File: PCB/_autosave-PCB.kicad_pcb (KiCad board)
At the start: 2 copper layers, 100 x 120 mm, 17 parts, among them SW1 SW_Push, SW2 SW_Push, SW3 SW_Push, SW4 SW_Push, SW5 SW_Push, SW6 SW_Push, U1 NodeMCU_1.0_(ESP-12E)

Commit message: Updated schematic after CMZ feedback
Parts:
- added H1: MountingHole_Pad, MountingHole:MountingHole_3.2mm_M3, F.Cu at (183.5, 30.1)
- added H2: MountingHole_Pad, MountingHole:MountingHole_3.2mm_M3, F.Cu at (91.5, 30.1)
- added H3: MountingHole_Pad, MountingHole:MountingHole_3.2mm_M3, F.Cu at (183.6, 142.1)
- added H4: MountingHole_Pad, MountingHole:MountingHole_3.2mm_M3, F.Cu at (91.5, 142.1)
- renumbered NHD to NHD-C12864A1Z-FSW-FBW-HTT1
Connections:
- net /Analog buttons renamed BUTTONS
- net Net-(BZ1-+) renamed BUZZER
- net Net-(NHD-C12864A1Z-FSW-FBW-HTT1-A0) renamed A0
- net Net-(NHD-C12864A1Z-FSW-FBW-HTT1-LED+) renamed 3.3 (16)
- net Net-(NHD-C12864A1Z-FSW-FBW-HTT1-SCL) renamed SCL
- net Net-(NHD-C12864A1Z-FSW-FBW-HTT1-SI) renamed SI
- net Net-(NHD-C12864A1Z-FSW-FBW-HTT1-VDD) renamed 3.3 (25)
- net Net-(NHD-C12864A1Z-FSW-FBW-HTT1-~{CS}) renamed ~{CS}
- net Net-(U1-RX(DPIO3)) renamed SW1
- net Net-(U1-TX(GPIO1)) renamed SW2
- net VCC renamed +5V
- D1 pad 2: Net-(D1-A) -> RED
- D2 pad 2: Net-(D2-A) -> GREEN
- EM4100 pad 1: Net-(EM4100-TX) -> HV2
- EM4100 pad 2: Net-(EM4100-RX) -> HV1
- NHD-C12864A1Z-FSW-FBW-HTT1 pad 5: Net-(NHD-C12864A1Z-FSW-FBW-HTT1-~{RESET}) -> ~{RESET}
- U1 pad 26: Net-(D2-A) -> ~{RESET}
- U1 pad 27: Net-(D1-A) -> LV2
- U1 pad 28: Net-(NHD-C12864A1Z-FSW-FBW-HTT1-~{RESET}) -> LV1
- U1 pad 30: unconnected-(U1-D0(GPIO16)-Pad30) -> RED
- U1 pad 4: Net-(EM4100-TX) -> GREEN
- U1 pad 5: Net-(EM4100-RX) -> unconnected-(U1-SD2(GPIO9)-Pad5)
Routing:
- net (no net): track 0.00 -> 272.7 mm
- net Net-(D1-A): track 139.3 -> 0.00 mm
- net Net-(D2-A): track 133.4 -> 0.00 mm
- net ~{RESET}: track 0.00 -> 92.2 mm
- net Net-(NHD-C12864A1Z-FSW-FBW-HTT1-~{RESET}): track 92.2 -> 0.00 mm
- net Net-(EM4100-TX): track 67.0 -> 0.00 mm
- net Net-(EM4100-RX): track 61.9 -> 0.00 mm
- net HV2: track 0.00 -> 59.7 mm
- net +5V: track 44.4 -> 0.28 mm
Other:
- outline, holes or cut-outs redrawn

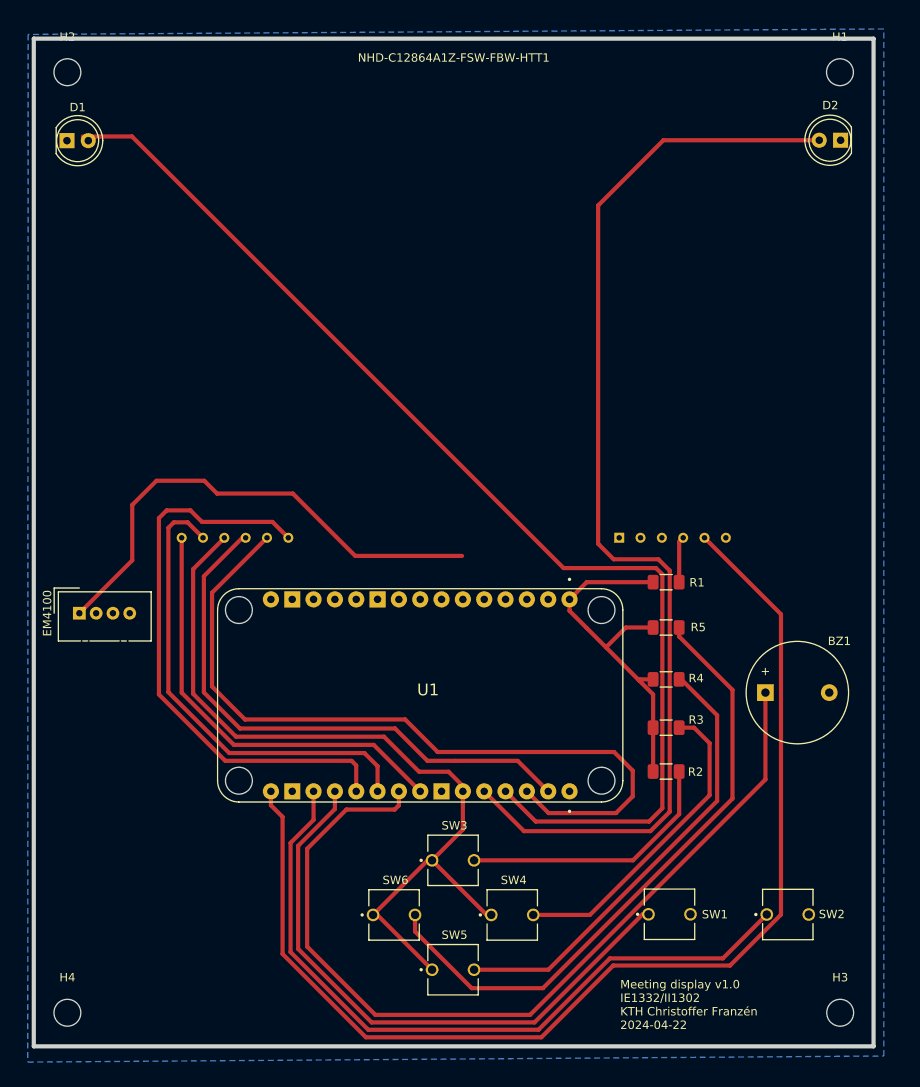
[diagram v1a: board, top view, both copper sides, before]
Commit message: drawn new PCB based on feedback
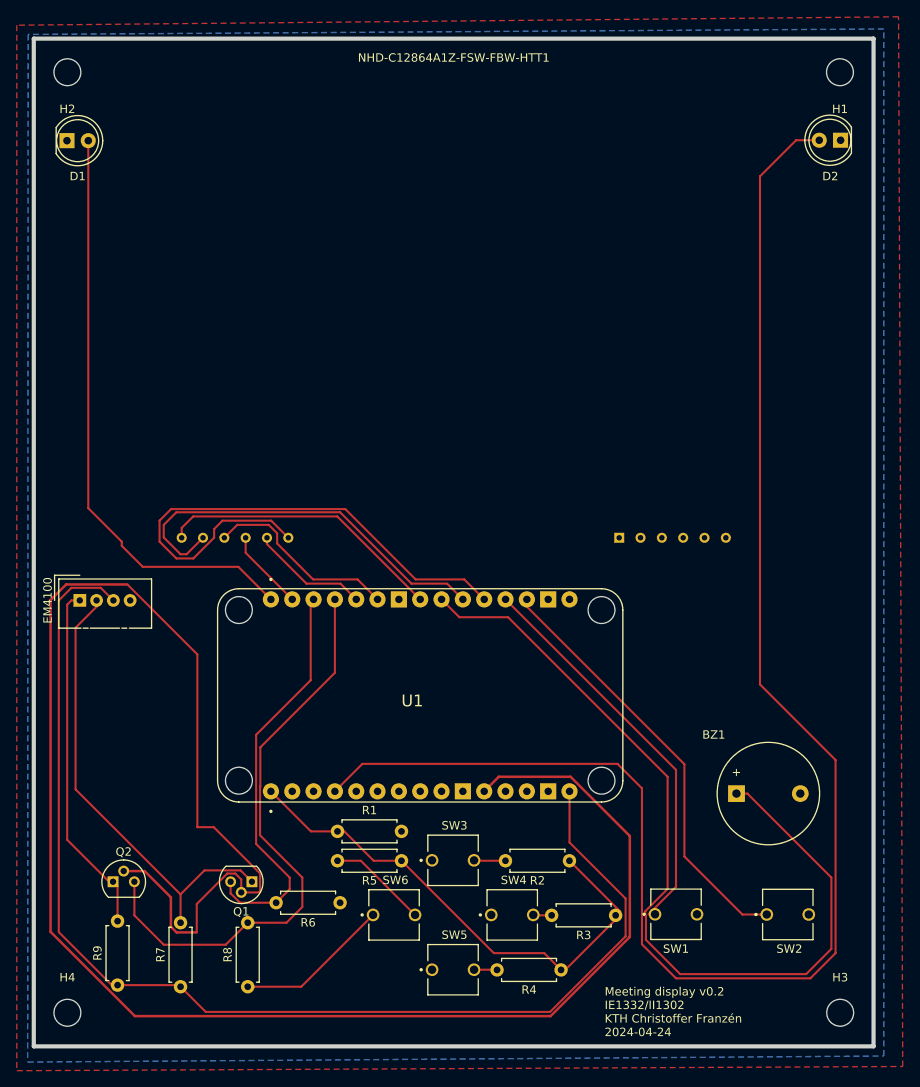
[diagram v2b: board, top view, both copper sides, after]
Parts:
- added Q1: NMOS, Package_TO_SOT_THT:TO-92, F.Cu at (113.5, 126.5)
- added Q2: NMOS, Package_TO_SOT_THT:TO-92, F.Cu at (97.0, 126.5)
- added R6: 10k, Resistor_THT:R_Axial_DIN0207_L6.3mm_D2.5mm_P7.62mm_Horizontal, F.Cu at (124.0, 129.0)
- added R7: 10k, Resistor_THT:R_Axial_DIN0207_L6.3mm_D2.5mm_P7.62mm_Horizontal, F.Cu at (105.0, 139.0)
- added R8: 10k, Resistor_THT:R_Axial_DIN0207_L6.3mm_D2.5mm_P7.62mm_Horizontal, F.Cu at (113.0, 139.0)
- added R9: 10k, Resistor_THT:R_Axial_DIN0207_L6.3mm_D2.5mm_P7.62mm_Horizontal, F.Cu at (97.5, 138.8)
- R1, R2, R3, R4, R5: footprint Resistor_SMD:R_1206_3216Metric_Pad1.30x1.75mm_HandSolder -> Resistor_THT:R_Axial_DIN0207_L6.3mm_D2.5mm_P7.62mm_Horizontal
- moved R1 43.3 mm to (131.3, 120.5)
- moved R5 42.0 mm to (131.3, 124.0), turned to 180 degrees
- moved R4 36.8 mm to (150.3, 137.0), turned to 180 degrees
- moved R3 23.1 mm to (156.8, 130.5), turned to 180 degrees
- moved R2 15.7 mm to (151.3, 124.0), turned to 180 degrees
- moved BZ1 12.5 mm to (171.2, 116.0)
- moved EM4100 1.53 mm to (93.0, 93.0)
- moved SW1 0.78 mm to (164.0, 130.4)
- turned U1 to 90 degrees
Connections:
- NHD-C12864A1Z-FSW-FBW-HTT1 pad 11: 3.3 (16) -> +3.3V
- NHD-C12864A1Z-FSW-FBW-HTT1 pad 3: 3.3 (25) -> +3.3V
- SW3 pad 1: 3.3 (25) -> +3.3V
- SW4 pad 1: 3.3 (25) -> +3.3V
- SW5 pad 1: 3.3 (25) -> +3.3V
- SW6 pad 1: 3.3 (25) -> +3.3V
- U1 pad 10: unconnected-(U1-GND-Pad10) -> GND
- U1 pad 11: unconnected-(U1-3.3V-Pad11) -> +3.3V
- U1 pad 16: 3.3 (16) -> +3.3V
- U1 pad 25: 3.3 (25) -> +3.3V
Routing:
- net +3.3V: track 0.00 -> 273.5 mm
- net (no net): track 272.7 -> 0.00 mm
- net GREEN: track 0.00 -> 188.7 mm
- net +5V: track 0.28 -> 142.9 mm
- net 3.3 (16): track 138.1 -> 0.00 mm
- net 3.3 (25): track 96.9 -> 0.00 mm
- net ~{RESET}: track 92.2 -> 14.1 mm
- net RED: track 0.00 -> 70.3 mm
- net LV2: track 0.00 -> 69.7 mm
- net Net-(R5-Pad2): track 74.9 -> 11.9 mm
- net A0: track 66.6 -> 9.63 mm
- net HV1: track 0.00 -> 54.8 mm
- net Net-(R4-Pad2): track 53.8 -> 2.75 mm
- net LV1: track 0.00 -> 48.5 mm
- net SW2: track 86.5 -> 51.1 mm
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- added copper zone on F.Cu, net +3.3V
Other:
- board text added: "Meeting display v0.2 IE1332/II1302 KTH Christoffer Franzén 2024-04-24"
- board text removed: "Meeting display v1.0 IE1332/II1302 KTH Christoffer Franzén 2024-04-22"
